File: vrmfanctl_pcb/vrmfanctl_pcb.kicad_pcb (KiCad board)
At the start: 2 copper layers, 25.6 x 20.6 mm, 11 parts, among them J1 SATA Power Male, J3 Pin header L-type male, J4 Pin header L-type female, Q1 ?, U1 ATtiny85-20PU

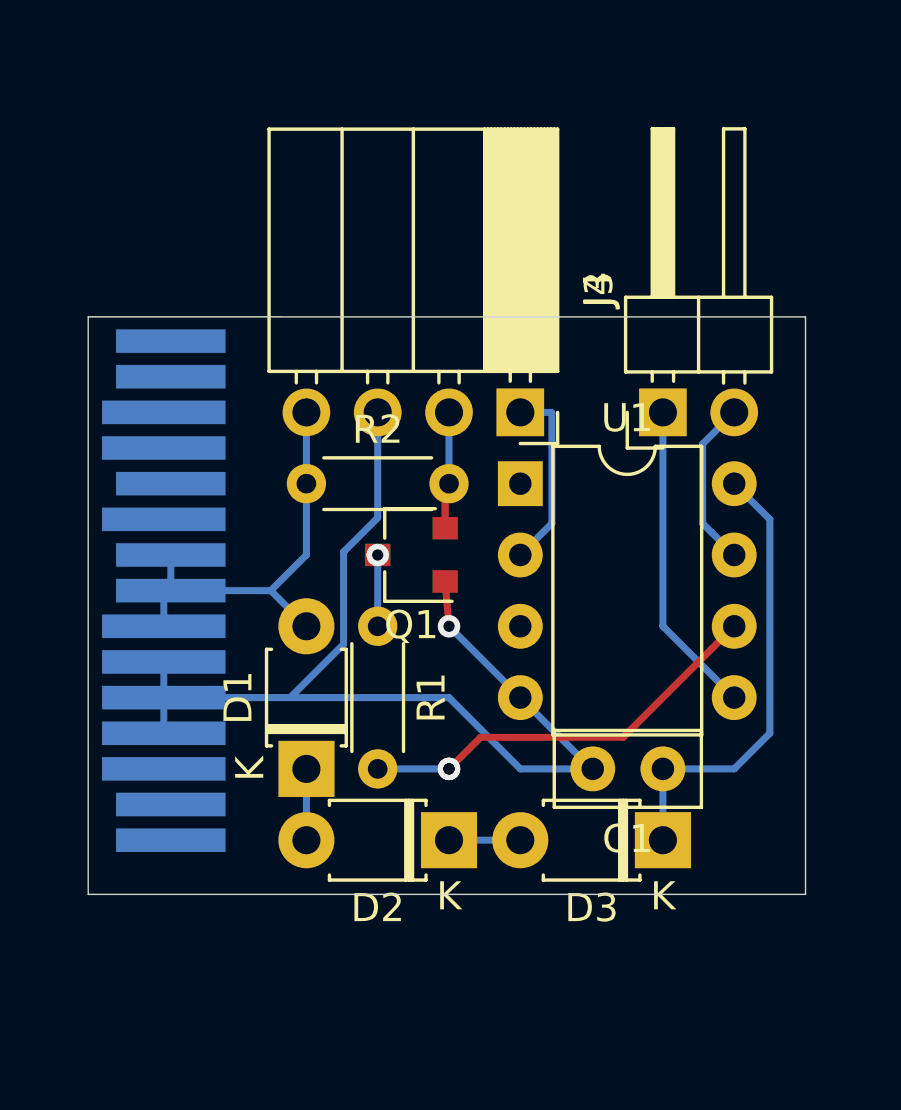
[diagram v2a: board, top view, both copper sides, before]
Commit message: supply 3.3V with M.2 SSD
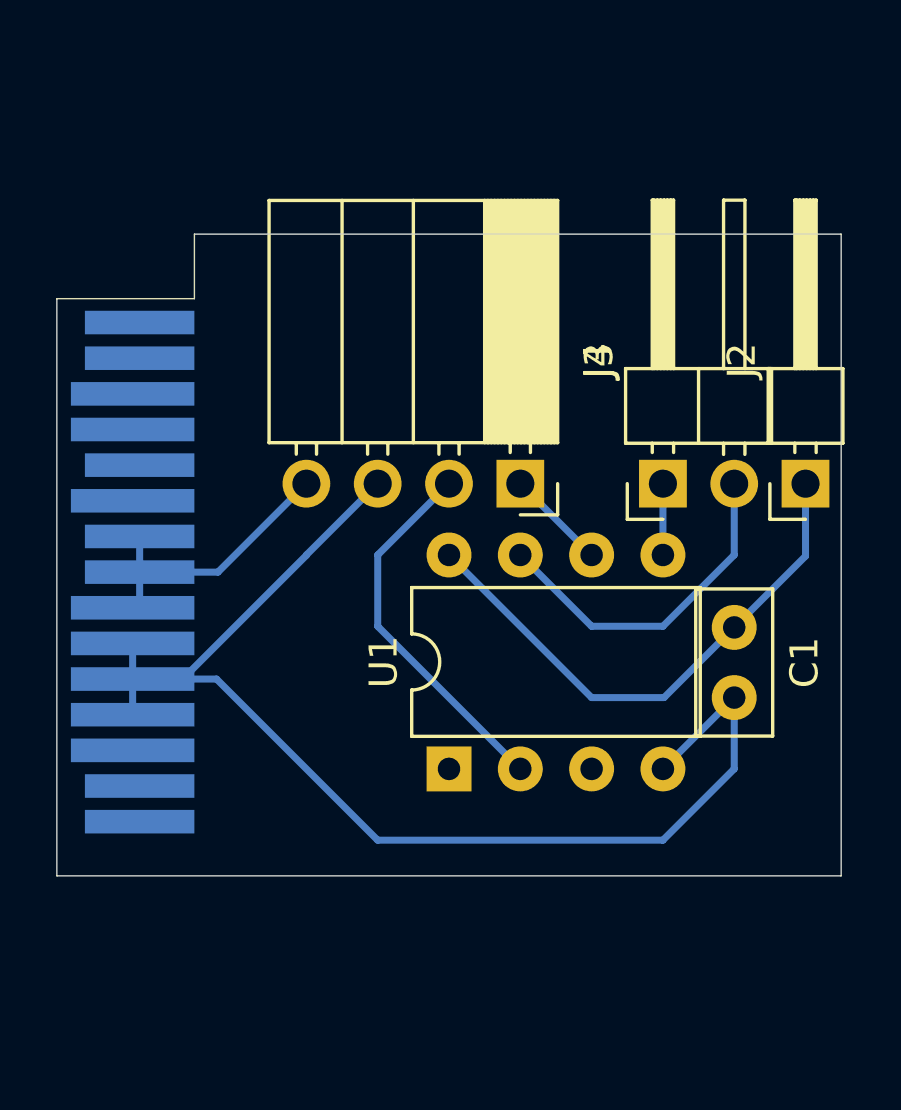
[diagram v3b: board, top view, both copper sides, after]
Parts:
- removed D1, D2, D3: D, Diode_THT:D_T-1_P5.08mm_Horizontal
- removed Q1: ?, Package_TO_SOT_SMD:SC-59
- removed R1: 2M, Resistor_THT:R_Axial_DIN0204_L3.6mm_D1.6mm_P5.08mm_Horizontal
- removed R2: 47K, Resistor_THT:R_Axial_DIN0204_L3.6mm_D1.6mm_P5.08mm_Horizontal
- added J2: Pin header L-shape male, Connector_PinHeader_2.54mm:PinHeader_1x01_P2.54mm_Horizontal, F.Cu at (63.5, 48.3)
- J3: value Pin header L-type male -> Pin header L-shape male
- J4: value Pin header L-type female -> Pin header L-shape female
- moved U1 10.5 mm to (50.8, 58.4), turned to 90 degrees
- moved C1 5.64 mm to (61.0, 53.4), turned to 270 degrees
- moved J3 2.54 mm to (58.4, 48.3)
- moved J4 2.54 mm to (53.3, 48.3)
- moved J1 1.29 mm to (41.7, 60.7)
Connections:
- J4 pad 1: /FG -> /PWM
- J4 pad 2: /PWM_5V -> /FG
- U1 pad 6: /PWM# -> /PWM
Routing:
- net /PWM#: track 14.8 -> 0.00 mm, vias 2 -> 0
- net /SDA: track 11.2 -> 2.54 mm
- net /5V: track 17.4 -> 9.89 mm
- net GND: track 39.6 -> 46.9 mm, vias 1 -> 0
- net /FG: track 6.66 -> 13.3 mm
- net /SCL: track 6.01 -> 12.3 mm
- net /PWM_5V: track 4.19 -> 0.00 mm
- net /PWM: track 0.00 -> 3.59 mm
- net VCC: track 16.3 -> 19.5 mm
- net Net-(Q1-Pad3): track 2.54 -> 0.00 mm, vias 1 -> 0
- net Net-(D2-Pad1): track 2.54 -> 0.00 mm
- net Net-(D1-Pad1): track 2.54 -> 0.00 mm
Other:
- board size 25.6 x 20.6 mm -> 27.9 x 22.9 mm

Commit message: Add a UART header. remove an I2C interface. Add a temperature sensor.
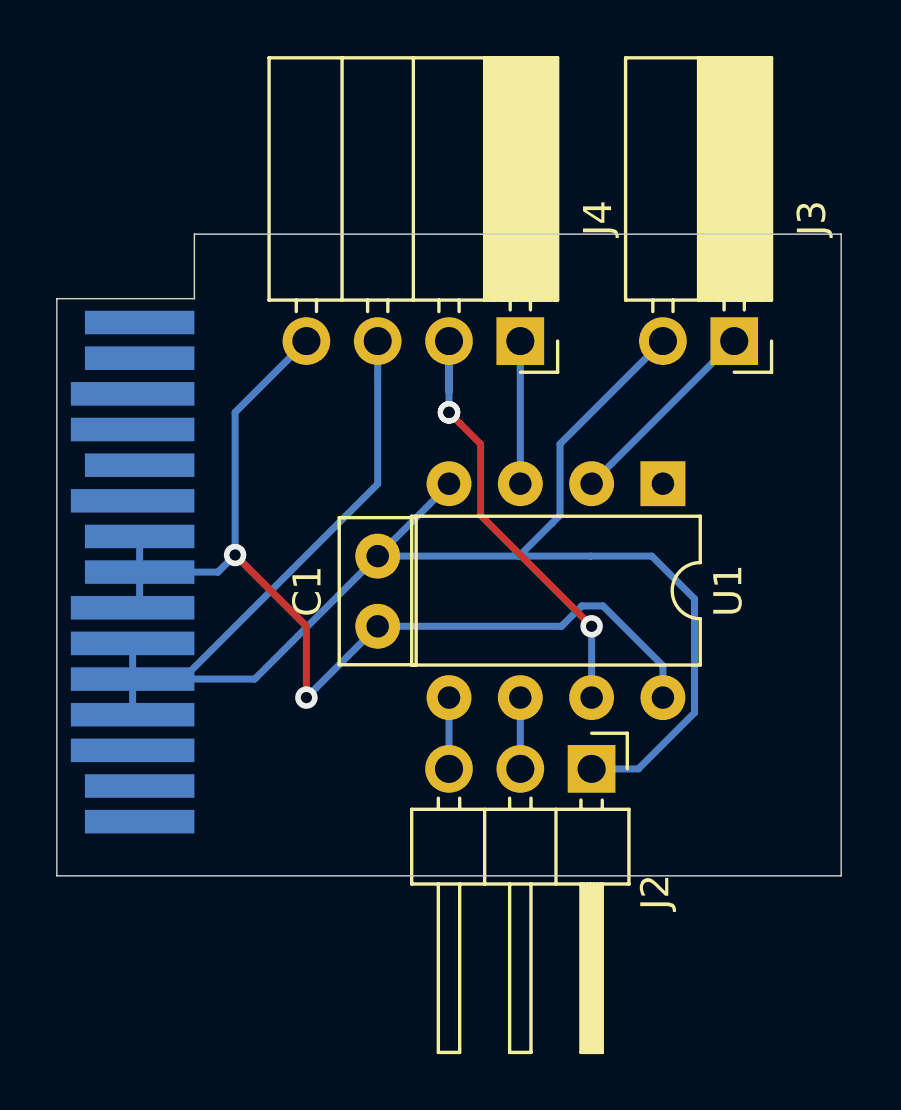
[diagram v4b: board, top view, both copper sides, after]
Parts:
- J2: value Pin header L-shape male -> Pin header L-shape; footprint Connector_PinHeader_2.54mm:PinHeader_1x01_P2.54mm_Horizontal -> Connector_PinHeader_2.54mm:PinHeader_1x03_P2.54mm_Horizontal
- J3: value Pin header L-shape male -> Pin socket L-shape; footprint Connector_PinHeader_2.54mm:PinHeader_1x02_P2.54mm_Horizontal -> Connector_PinSocket_2.54mm:PinSocket_1x02_P2.54mm_Horizontal
- J4: value Pin header L-shape female -> Pin socket L-shape
- moved C1 12.7 mm to (48.3, 53.3), turned to 90 degrees
- moved U1 12.7 mm to (58.4, 48.3), turned to 270 degrees
- moved J2 12.7 mm to (55.9, 58.4), turned to 270 degrees
- moved J3 5.68 mm to (61.0, 43.2), turned to 270 degrees
- moved J4 5.08 mm to (53.3, 43.2)
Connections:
- J1 pad 1: Net-(J1-Pad1) -> (no net)
- J1 pad 10: Net-(J1-Pad10) -> (no net)
- J1 pad 11: Net-(J1-Pad11) -> (no net)
- J1 pad 12: Net-(J1-Pad12) -> (no net)
- J1 pad 13: Net-(J1-Pad13) -> (no net)
- J1 pad 14: Net-(J1-Pad14) -> (no net)
- J1 pad 15: Net-(J1-Pad15) -> (no net)
- J1 pad 2: Net-(J1-Pad2) -> (no net)
- J1 pad 3: Net-(J1-Pad3) -> (no net)
- J1 pad 7: /5V -> VCC
- J1 pad 8: /5V -> VCC
- J1 pad 9: /5V -> VCC
- J2 pad 1: VCC -> GND
- J3 pad 1: /SDA -> /TEMP
- J3 pad 2: /SCL -> GND
- J4 pad 4: /5V -> VCC
- U1 pad 1: Net-(U1-Pad1) -> (no net)
- U1 pad 2: /FG -> /TEMP
- U1 pad 3: Net-(U1-Pad3) -> /PWM
- U1 pad 5: /SDA -> /TX
- U1 pad 6: /PWM -> /RX
- U1 pad 7: /SCL -> /FG
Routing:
- net VCC: track 19.5 -> 38.7 mm, vias 0 -> 2
- net GND: track 46.9 -> 65.4 mm
- net /SCL: track 12.3 -> 0.00 mm
- net /5V: track 9.89 -> 0.00 mm
- net /TEMP: track 0.00 -> 7.18 mm
- net /FG: track 13.3 -> 16.6 mm, vias 0 -> 3
- net /TX: track 0.00 -> 2.54 mm
- net /SDA: track 2.54 -> 0.00 mm
- net /RX: track 0.00 -> 2.54 mm
- net /PWM: track 3.59 -> 5.08 mm

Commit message: Use through hole instead of pin header
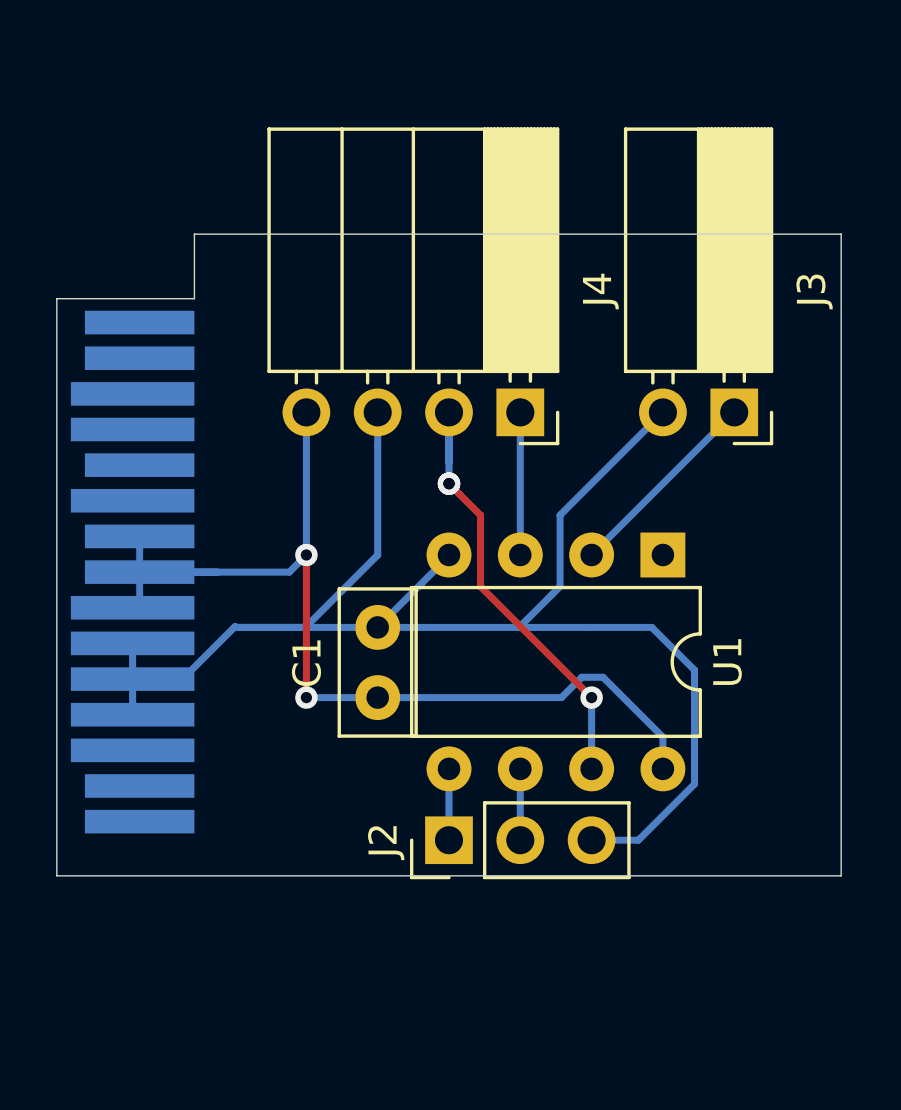
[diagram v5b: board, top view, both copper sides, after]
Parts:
- J2: value Pin header L-shape -> Hole; footprint Connector_PinHeader_2.54mm:PinHeader_1x03_P2.54mm_Horizontal -> Connector_PinHeader_2.54mm:PinHeader_1x03_P2.54mm_Vertical
- moved J2 5.68 mm to (50.8, 61.0), turned to 90 degrees
- moved C1 2.54 mm to (48.3, 55.9)
- moved J3 2.54 mm to (61.0, 45.7)
- moved J4 2.54 mm to (53.3, 45.7)
- moved U1 2.54 mm to (58.4, 50.8)
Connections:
- net /TEMP renamed /D+
- J1 pad 1: (no net) -> Net-(J1-Pad1)
- J1 pad 10: (no net) -> Net-(J1-Pad10)
- J1 pad 11: (no net) -> Net-(J1-Pad11)
- J1 pad 12: (no net) -> Net-(J1-Pad12)
- J1 pad 13: (no net) -> Net-(J1-Pad13)
- J1 pad 14: (no net) -> Net-(J1-Pad14)
- J1 pad 15: (no net) -> Net-(J1-Pad15)
- J1 pad 2: (no net) -> Net-(J1-Pad2)
- J1 pad 3: (no net) -> Net-(J1-Pad3)
- J2 pad 1: GND -> /TX
- J2 pad 3: /TX -> GND
- U1 pad 1: (no net) -> Net-(U1-Pad1)
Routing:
- net GND: track 65.4 -> 58.9 mm

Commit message: remove unneeded FG wire
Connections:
- J4 pad 2: /FG -> Net-(J4-Pad2)
- U1 pad 7: /FG -> Net-(U1-Pad7)
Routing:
- net /FG: track 16.6 -> 0.00 mm, vias 3 -> 0
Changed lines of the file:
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@@
     (thickness 1.6)
     (drawings 6)
-    (tracks 57)
+    (tracks 44)
     (zones 0)
     (modules 6)
-    (nets 18)
+    (nets 19)
   )
   (page A4)
@@
   (net 1 VCC)
   (net 2 GND)
-  (net 3 /FG)
-  (net 4 /PWM)
-  (net 5 /RX)
-  (net 6 /TX)
-  (net 7 "Net-(J1-Pad15)")
-  (net 8 "Net-(J1-Pad14)")
-  (net 9 "Net-(J1-Pad13)")
-  (net 10 "Net-(J1-Pad12)")
-  (net 11 "Net-(J1-Pad11)")
-  (net 12 "Net-(J1-Pad10)")
-  (net 13 "Net-(J1-Pad3)")
-  (net 14 "Net-(J1-Pad2)")
-  (net 15 "Net-(J1-Pad1)")
-  (net 16 /D+)
-  (net 17 "Net-(U1-Pad1)")
+  (net 3 /PWM)
+  (net 4 /RX)
+  (net 5 /TX)
+  (net 6 "Net-(J1-Pad15)")
+  (net 7 "Net-(J1-Pad14)")
+  (net 8 "Net-(J1-Pad13)")
+  (net 9 "Net-(J1-Pad12)")
+  (net 10 "Net-(J1-Pad11)")
+  (net 11 "Net-(J1-Pad10)")
+  (net 12 "Net-(J1-Pad3)")
+  (net 13 "Net-(J1-Pad2)")
+  (net 14 "Net-(J1-Pad1)")
+  (net 15 /D+)
+  (net 16 "Net-(U1-Pad1)")
+  (net 17 "Net-(J4-Pad2)")
+  (net 18 "Net-(U1-Pad7)")
   (net_class Default "これはデフォルトのネット クラスです。"
     (clearance 0.2)
@@
     (uvia_drill 0.1)
     (add_net /D+)
-    (add_net /FG)
     (add_net /PWM)
     (add_net /RX)
@@
     (add_net "Net-(J1-Pad2)")
     (add_net "Net-(J1-Pad3)")
+    (add_net "Net-(J4-Pad2)")
     (add_net "Net-(U1-Pad1)")
+    (add_net "Net-(U1-Pad7)")
     (add_net VCC)
   )
@@
       (net 2 GND))
     (pad 7 thru_hole oval (at 7.62 2.54 270) (size 1.6 1.6) (drill 0.8) (layers *.Cu *.Mask)
-      (net 3 /FG))
+      (net 18 "Net-(U1-Pad7)"))
     (pad 3 thru_hole oval (at 0 5.08 270) (size 1.6 1.6) (drill 0.8) (layers *.Cu *.Mask)
-      (net 4 /PWM))
+      (net 3 /PWM))
     (pad 6 thru_hole oval (at 7.62 5.08 270) (size 1.6 1.6) (drill 0.8) (layers *.Cu *.Mask)
-      (net 5 /RX))
+      (net 4 /RX))
     (pad 2 thru_hole oval (at 0 2.54 270) (size 1.6 1.6) (drill 0.8) (layers *.Cu *.Mask)
-      (net 16 /D+))
+      (net 15 /D+))
     (pad 5 thru_hole oval (at 7.62 7.62 270) (size 1.6 1.6) (drill 0.8) (layers *.Cu *.Mask)
-      (net 6 /TX))
+      (net 5 /TX))
     (pad 1 thru_hole rect (at 0 0 270) (size 1.6 1.6) (drill 0.8) (layers *.Cu *.Mask)
-      (net 17 "Net-(U1-Pad1)"))
+      (net 16 "Net-(U1-Pad1)"))
     (model ${KISYS3DMOD}/Package_DIP.3dshapes/DIP-8_W7.62mm.wrl
       (at (xyz 0 0 0))
@@
     (fp_line (start 1.52 0) (end -19.05 0) (layer B.SilkS) (width 0.12))
     (pad 15 smd rect (at -18.2 1.95 270) (size 0.84 3.9) (layers B.Cu B.Paste B.Mask)
-      (net 7 "Net-(J1-Pad15)"))
+      (net 6 "Net-(J1-Pad15)"))
     (pad 14 smd rect (at -16.93 1.95 270) (size 0.84 3.9) (layers B.Cu B.Paste B.Mask)
-      (net 8 "Net-(J1-Pad14)"))
+      (net 7 "Net-(J1-Pad14)"))
     (pad 13 smd rect (at -15.66 2.2 270) (size 0.84 4.4) (layers B.Cu B.Paste B.Mask)
-      (net 9 "Net-(J1-Pad13)"))
+      (net 8 "Net-(J1-Pad13)"))
     (pad 12 smd rect (at -14.39 2.2 270) (size 0.84 4.4) (layers B.Cu B.Paste B.Mask)
-      (net 10 "Net-(J1-Pad12)"))
+      (net 9 "Net-(J1-Pad12)"))
     (pad 11 smd rect (at -13.12 1.95 270) (size 0.84 3.9) (layers B.Cu B.Paste B.Mask)
-      (net 11 "Net-(J1-Pad11)"))
+      (net 10 "Net-(J1-Pad11)"))
     (pad 10 smd rect (at -11.85 2.2 270) (size 0.84 4.4) (layers B.Cu B.Paste B.Mask)
-      (net 12 "Net-(J1-Pad10)"))
+      (net 11 "Net-(J1-Pad10)"))
     (pad 9 smd rect (at -10.58 1.95 270) (size 0.84 3.9) (layers B.Cu B.Paste B.Mask)
       (net 1 VCC))
@@
       (net 2 GND))
     (pad 3 smd rect (at -2.96 2.2 270) (size 0.84 4.4) (layers B.Cu B.Paste B.Mask)
-      (net 13 "Net-(J1-Pad3)"))
+      (net 12 "Net-(J1-Pad3)"))
     (pad 2 smd rect (at -1.69 1.95 270) (size 0.84 3.9) (layers B.Cu B.Paste B.Mask)
-      (net 14 "Net-(J1-Pad2)"))
+      (net 13 "Net-(J1-Pad2)"))
     (pad 1 smd rect (at -0.42 1.95 270) (size 0.84 3.9) (layers B.Cu B.Paste B.Mask)
-      (net 15 "Net-(J1-Pad1)"))
+      (net 14 "Net-(J1-Pad1)"))
   )
   (module Connector_PinSocket_2.54mm:PinSocket_1x02_P2.54mm_Horizontal (layer F.Cu)
@@
     )
     (pad 1 thru_hole rect (at 0 0 270) (size 1.7 1.7) (drill 1) (layers *.Cu *.Mask)
-      (net 16 /D+))
+      (net 15 /D+))
     (pad 2 thru_hole oval (at 0 2.54 270) (size 1.7 1.7) (drill 1) (layers *.Cu *.Mask)
       (net 2 GND))
@@
     )
     (pad 1 thru_hole rect (at 0 0 270) (size 1.7 1.7) (drill 1) (layers *.Cu *.Mask)
-      (net 4 /PWM))
+      (net 3 /PWM))
     (pad 2 thru_hole oval (at 0 2.54 270) (size 1.7 1.7) (drill 1) (layers *.Cu *.Mask)
-      (net 3 /FG))
+      (net 17 "Net-(J4-Pad2)"))
     (pad 3 thru_hole oval (at 0 5.08 270) (size 1.7 1.7) (drill 1) (layers *.Cu *.Mask)
       (net 2 GND))
@@
     )
     (pad 1 thru_hole rect (at 0 0 90) (size 1.7 1.7) (drill 1) (layers *.Cu *.Mask)
-      (net 6 /TX))
+      (net 5 /TX))
     (pad 2 thru_hole oval (at 0 2.54 90) (size 1.7 1.7) (drill 1) (layers *.Cu *.Mask)
-      (net 5 /RX))
+      (net 4 /RX))
     (pad 3 thru_hole oval (at 0 5.08 90) (size 1.7 1.7) (drill 1) (layers *.Cu *.Mask)
       (net 2 GND))
@@
   (segment (start 45.68 53.38) (end 48.26 50.8) (width 0.25) (layer B.Cu) (net 2))
   (segment (start 43.21 53.38) (end 45.68 53.38) (width 0.25) (layer B.Cu) (net 2))
-  (segment (start 55.88 58.42) (end 55.88 55.88) (width 0.25) (layer B.Cu) (net 3))
-  (segment (start 55.88 55.88) (end 55.88 55.88) (width 0.25) (layer B.Cu) (net 3))
-  (via (at 55.88 55.88) (size 0.8) (drill 0.4) (layers F.Cu B.Cu) (net 3))
-  (segment (start 50.8 45.72) (end 50.8 47.534999) (width 0.25) (layer B.Cu) (net 3))
-  (segment (start 50.8 45.72) (end 50.8 48.26) (width 0.25) (layer B.Cu) (net 3))
-  (segment (start 50.8 48.26) (end 50.8 48.26) (width 0.25) (layer B.Cu) (net 3))
-  (via (at 50.8 48.26) (size 0.8) (drill 0.4) (layers F.Cu B.Cu) (net 3))
-  (segment (start 50.8 48.26) (end 50.8 48.26) (width 0.25) (layer B.Cu) (net 3))
-  (via (at 50.8 48.26) (size 0.8) (drill 0.4) (layers F.Cu B.Cu) (net 3))
-  (segment (start 51.199999 48.659999) (end 50.8 48.26) (width 0.25) (layer F.Cu) (net 3))
-  (segment (start 51.925001 49.385001) (end 51.199999 48.659999) (width 0.25) (layer F.Cu) (net 3))
-  (segment (start 51.925001 51.925001) (end 51.925001 49.385001) (width 0.25) (layer F.Cu) (net 3))
-  (segment (start 55.88 55.88) (end 51.925001 51.925001) (width 0.25) (layer F.Cu) (net 3))
-  (segment (start 53.34 45.72) (end 53.34 50.8) (width 0.25) (layer B.Cu) (net 4))
-  (segment (start 53.34 58.42) (end 53.34 60.96) (width 0.25) (layer B.Cu) (net 5))
-  (segment (start 50.8 58.42) (end 50.8 60.96) (width 0.25) (layer B.Cu) (net 6))
-  (segment (start 60.96 45.72) (end 55.88 50.8) (width 0.25) (layer B.Cu) (net 16))
+  (segment (start 53.34 45.72) (end 53.34 50.8) (width 0.25) (layer B.Cu) (net 3))
+  (segment (start 53.34 58.42) (end 53.34 60.96) (width 0.25) (layer B.Cu) (net 4))
+  (segment (start 50.8 58.42) (end 50.8 60.96) (width 0.25) (layer B.Cu) (net 5))
+  (segment (start 60.96 45.72) (end 55.88 50.8) (width 0.25) (layer B.Cu) (net 15))
 )
